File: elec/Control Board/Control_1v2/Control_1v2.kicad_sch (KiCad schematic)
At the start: 166 parts, among them J1 DB9_Female_MountingHoles, J10 Conn_02x12_Odd_Even, J11 Screw_Terminal_01x02, J14 Conn_01x10, J2 Conn_01x08, J25 Screw_Terminal_01x02, J26 Conn_01x10, J27 Conn_02x12_Odd_Even, J28 Screw_Terminal_01x02, J29 Conn_01x10, J3 Conn_01x08, J37 Conn_01x04, J4 Conn_01x08, J5 Conn_01x08, J6 Conn_01x08, J7 Conn_01x10, J8 Conn_02x18_Odd_Even, J9 Conn_01x10, Q601 BSS138

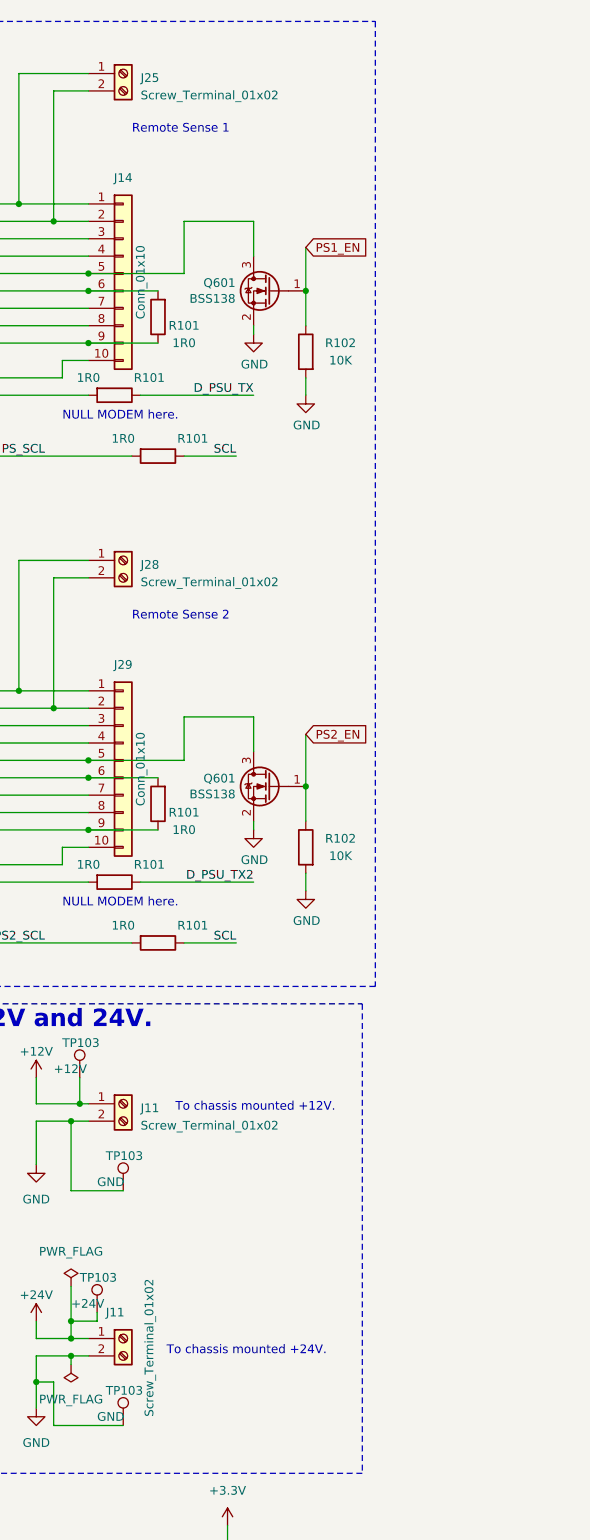
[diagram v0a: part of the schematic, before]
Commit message: Update Control_1v2.kicad_sch for correct JLCPCB part number on JST 2 pin XH Connector. Wire up J30 as connector for OEDCS Fan.
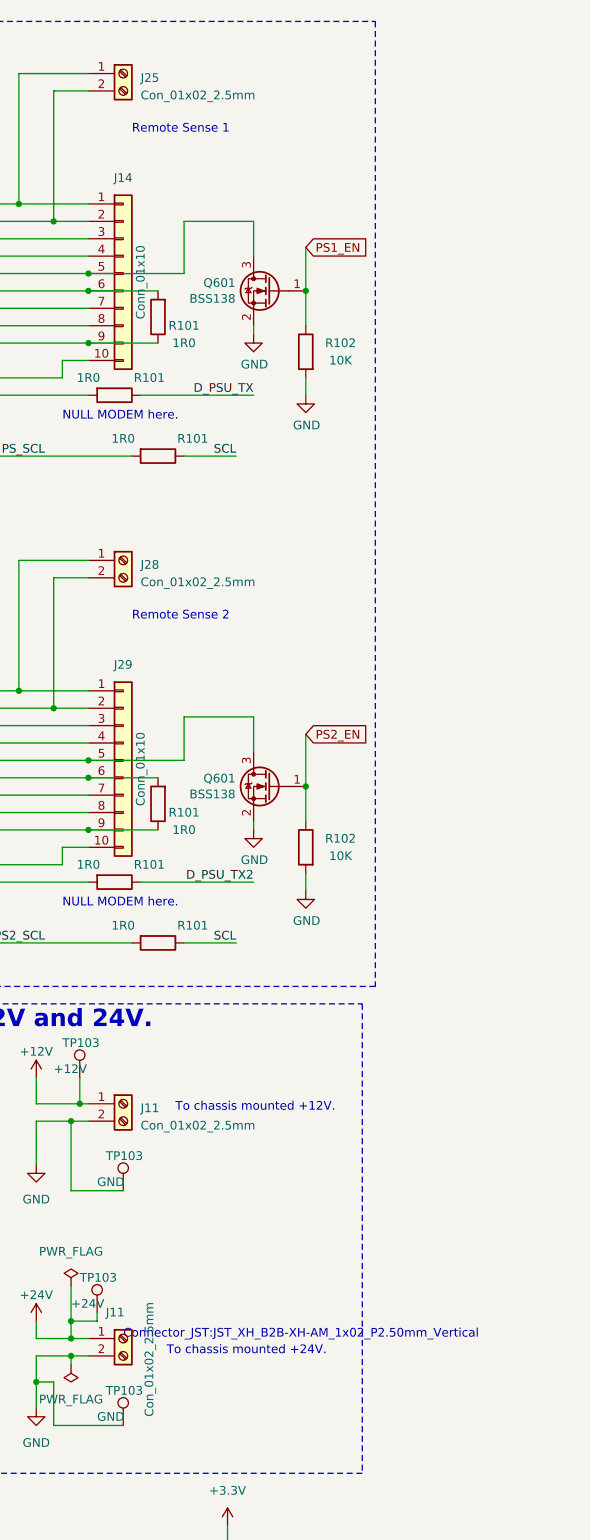
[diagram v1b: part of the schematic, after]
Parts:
- J11, J25, J28: value Screw_Terminal_01x02 -> Con_01x02_2.5mm; footprint TerminalBlock_TE-Connectivity:TerminalBlock_TE_282834-2_1x02_P2.54mm_Horizontal -> Connector_JST:JST_XH_B2B-XH-AM_1x02_P2.50mm_Vertical; Cost 0.1537 -> 0.2156; MPN DB125-2.54-2P-GN-S -> B2B-XH-A-GU; Manufacturer DIBO -> JST
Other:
- note added: "Connector_JST:JST_XH_B2B-XH-AM_1x02_P2.50mm_Vertical"
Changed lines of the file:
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@@
     (effects (font (size 2.54 2.54)) (justify left bottom))
   )
+  (text "Connector_JST:JST_XH_B2B-XH-AM_1x02_P2.50mm_Vertical\n"
+    (at 482.6 206.502 0)
+    (effects (font (size 1.27 1.27)) (justify left bottom))
+  )
   (text "V_ASSY_VERSIONING\nControl 1.2 voltage = 1.055V" (at 124.714 137.414 0)
     (effects (font (size 1.27 1.27)) (justify left bottom))
@@
       (effects (font (size 1.27 1.27)) (justify left))
     )
-    (property "Value" "Screw_Terminal_01x02" (at 486.41 217.805 90)
+    (property "Value" "Con_01x02_2.5mm" (at 486.41 217.805 90)
       (effects (font (size 1.27 1.27)) (justify left))
     )
-    (property "Footprint" "TerminalBlock_TE-Connectivity:TerminalBlock_TE_282834-2_1x02_P2.54mm_Horizontal" (at 482.6 206.375 0)
+    (property "Footprint" "Connector_JST:JST_XH_B2B-XH-AM_1x02_P2.50mm_Vertical" (at 482.6 206.375 0)
       (effects (font (size 1.27 1.27)) hide)
     )
@@
       (effects (font (size 1.27 1.27)) hide)
     )
-    (property "Cost" "0.1537" (at 482.6 206.375 0)
+    (property "Cost" "0.2156" (at 482.6 206.375 0)
       (effects (font (size 1.27 1.27)) hide)
     )
-    (property "Description" "1x2P XH 1 2.5mm 2 Brass Plugin,P=2.5mm Wire To Board / Wire To Wire Connector ROHS" (at 482.6 206.375 0)
+    (property "Description" "1x2P 2P XH Gold 2 -25℃~+85℃ 3A 1 2.5mm Brass Direct Insert Plugin,P=2.5mm Wire To Board Connector ROHS" (at 482.6 206.375 0)
       (effects (font (size 1.27 1.27)) hide)
     )
@@
       (effects (font (size 1.27 1.27)) hide)
     )
-    (property "MPN" "DB125-2.54-2P-GN-S" (at 482.6 206.375 0)
+    (property "MPN" "B2B-XH-A-GU" (at 482.6 206.375 0)
       (effects (font (size 1.27 1.27)) hide)
     )
-    (property "Manufacturer" "DIBO" (at 482.6 206.375 0)
+    (property "Manufacturer" "JST" (at 482.6 206.375 0)
       (effects (font (size 1.27 1.27)) hide)
     )
@@
       (effects (font (size 1.27 1.27)) (justify left))
     )
-    (property "Value" "Screw_Terminal_01x02" (at 485.14 175.26 0)
+    (property "Value" "Con_01x02_2.5mm" (at 485.14 175.26 0)
       (effects (font (size 1.27 1.27)) (justify left))
     )
-    (property "Footprint" "TerminalBlock_TE-Connectivity:TerminalBlock_TE_282834-2_1x02_P2.54mm_Horizontal" (at 482.6 172.085 0)
+    (property "Footprint" "Connector_JST:JST_XH_B2B-XH-AM_1x02_P2.50mm_Vertical" (at 482.6 172.085 0)
       (effects (font (size 1.27 1.27)) hide)
     )
@@
       (effects (font (size 1.27 1.27)) hide)
     )
-    (property "Cost" "0.1537" (at 482.6 172.085 0)
+    (property "Cost" "0.2156" (at 482.6 172.085 0)
       (effects (font (size 1.27 1.27)) hide)
     )
-    (property "Description" "1x2P XH 1 2.5mm 2 Brass Plugin,P=2.5mm Wire To Board / Wire To Wire Connector ROHS" (at 482.6 172.085 0)
+    (property "Description" "1x2P 2P XH Gold 2 -25℃~+85℃ 3A 1 2.5mm Brass Direct Insert Plugin,P=2.5mm Wire To Board Connector ROHS" (at 482.6 172.085 0)
       (effects (font (size 1.27 1.27)) hide)
     )
@@
       (effects (font (size 1.27 1.27)) hide)
     )
-    (property "MPN" "DB125-2.54-2P-GN-S" (at 482.6 172.085 0)
+    (property "MPN" "B2B-XH-A-GU" (at 482.6 172.085 0)
       (effects (font (size 1.27 1.27)) hide)
     )
-    (property "Manufacturer" "DIBO" (at 482.6 172.085 0)
+    (property "Manufacturer" "JST" (at 482.6 172.085 0)
       (effects (font (size 1.27 1.27)) hide)
     )
@@
       (effects (font (size 1.27 1.27)) (justify left))
     )
-    (property "Value" "Screw_Terminal_01x02" (at 485.14 24.765 0)
+    (property "Value" "Con_01x02_2.5mm" (at 485.14 24.765 0)
       (effects (font (size 1.27 1.27)) (justify left))
     )
-    (property "Footprint" "TerminalBlock_TE-Connectivity:TerminalBlock_TE_282834-2_1x02_P2.54mm_Horizontal" (at 482.6 21.59 0)
+    (property "Footprint" "Connector_JST:JST_XH_B2B-XH-AM_1x02_P2.50mm_Vertical" (at 482.6 21.59 0)
       (effects (font (size 1.27 1.27)) hide)
     )
@@
       (effects (font (size 1.27 1.27)) hide)
     )
-    (property "Cost" "0.1537" (at 482.6 21.59 0)
+    (property "Cost" "0.2156" (at 482.6 21.59 0)
       (effects (font (size 1.27 1.27)) hide)
     )
-    (property "Description" "1x2P XH 1 2.5mm 2 Brass Plugin,P=2.5mm Wire To Board / Wire To Wire Connector ROHS" (at 482.6 21.59 0)
+    (property "Description" "1x2P 2P XH Gold 2 -25℃~+85℃ 3A 1 2.5mm Brass Direct Insert Plugin,P=2.5mm Wire To Board Connector ROHS" (at 482.6 21.59 0)
       (effects (font (size 1.27 1.27)) hide)
     )
@@
       (effects (font (size 1.27 1.27)) hide)
     )
-    (property "MPN" "DB125-2.54-2P-GN-S" (at 482.6 21.59 0)
+    (property "MPN" "B2B-XH-A-GU" (at 482.6 21.59 0)
       (effects (font (size 1.27 1.27)) hide)
     )
-    (property "Manufacturer" "DIBO" (at 482.6 21.59 0)
+    (property "Manufacturer" "JST" (at 482.6 21.59 0)
       (effects (font (size 1.27 1.27)) hide)
     )
@@
       (effects (font (size 1.27 1.27)) (justify left))
     )
-    (property "Value" "Screw_Terminal_01x02" (at 485.14 95.885 0)
+    (property "Value" "Con_01x02_2.5mm" (at 485.14 95.885 0)
       (effects (font (size 1.27 1.27)) (justify left))
     )
-    (property "Footprint" "TerminalBlock_TE-Connectivity:TerminalBlock_TE_282834-2_1x02_P2.54mm_Horizontal" (at 482.6 92.71 0)
+    (property "Footprint" "Connector_JST:JST_XH_B2B-XH-AM_1x02_P2.50mm_Vertical" (at 482.6 92.71 0)
       (effects (font (size 1.27 1.27)) hide)
     )
@@
       (effects (font (size 1.27 1.27)) hide)
     )
-    (property "Cost" "0.1537" (at 482.6 92.71 0)
+    (property "Cost" "0.2156" (at 482.6 92.71 0)
       (effects (font (size 1.27 1.27)) hide)
     )
-    (property "Description" "1x2P XH 1 2.5mm 2 Brass Plugin,P=2.5mm Wire To Board / Wire To Wire Connector ROHS" (at 482.6 92.71 0)
+    (property "Description" "1x2P 2P XH Gold 2 -25℃~+85℃ 3A 1 2.5mm Brass Direct Insert Plugin,P=2.5mm Wire To Board Connector ROHS" (at 482.6 92.71 0)
       (effects (font (size 1.27 1.27)) hide)
     )
@@
       (effects (font (size 1.27 1.27)) hide)
     )
-    (property "MPN" "DB125-2.54-2P-GN-S" (at 482.6 92.71 0)
+    (property "MPN" "B2B-XH-A-GU" (at 482.6 92.71 0)
       (effects (font (size 1.27 1.27)) hide)
     )
-    (property "Manufacturer" "DIBO" (at 482.6 92.71 0)
+    (property "Manufacturer" "JST" (at 482.6 92.71 0)
       (effects (font (size 1.27 1.27)) hide)
     )

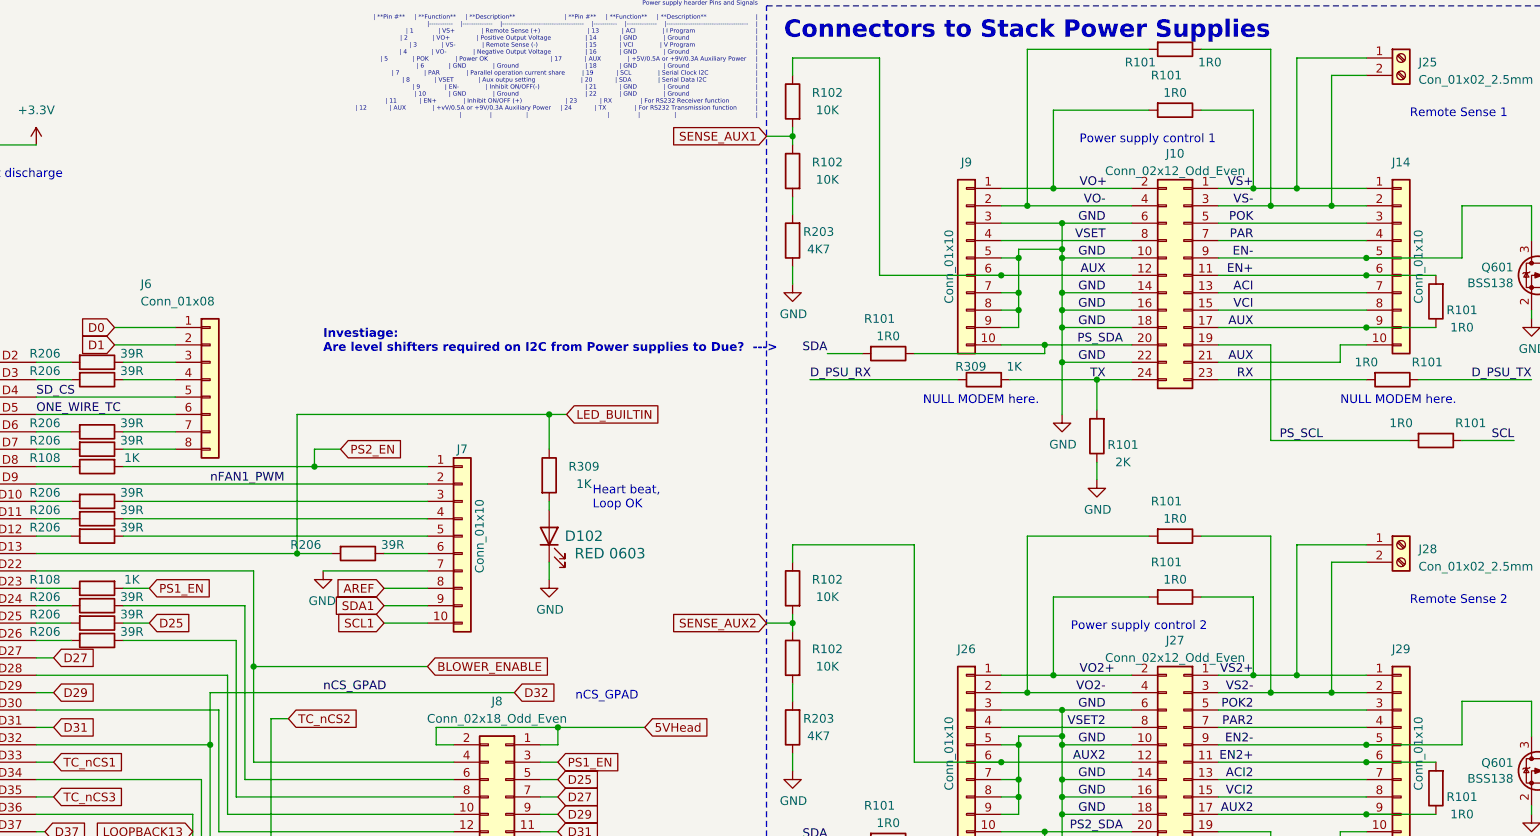
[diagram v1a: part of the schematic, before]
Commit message: Update Control_1v2.kicad_sch for Power OK from power supply into Due for possible interupt service of power supply NOT OK.
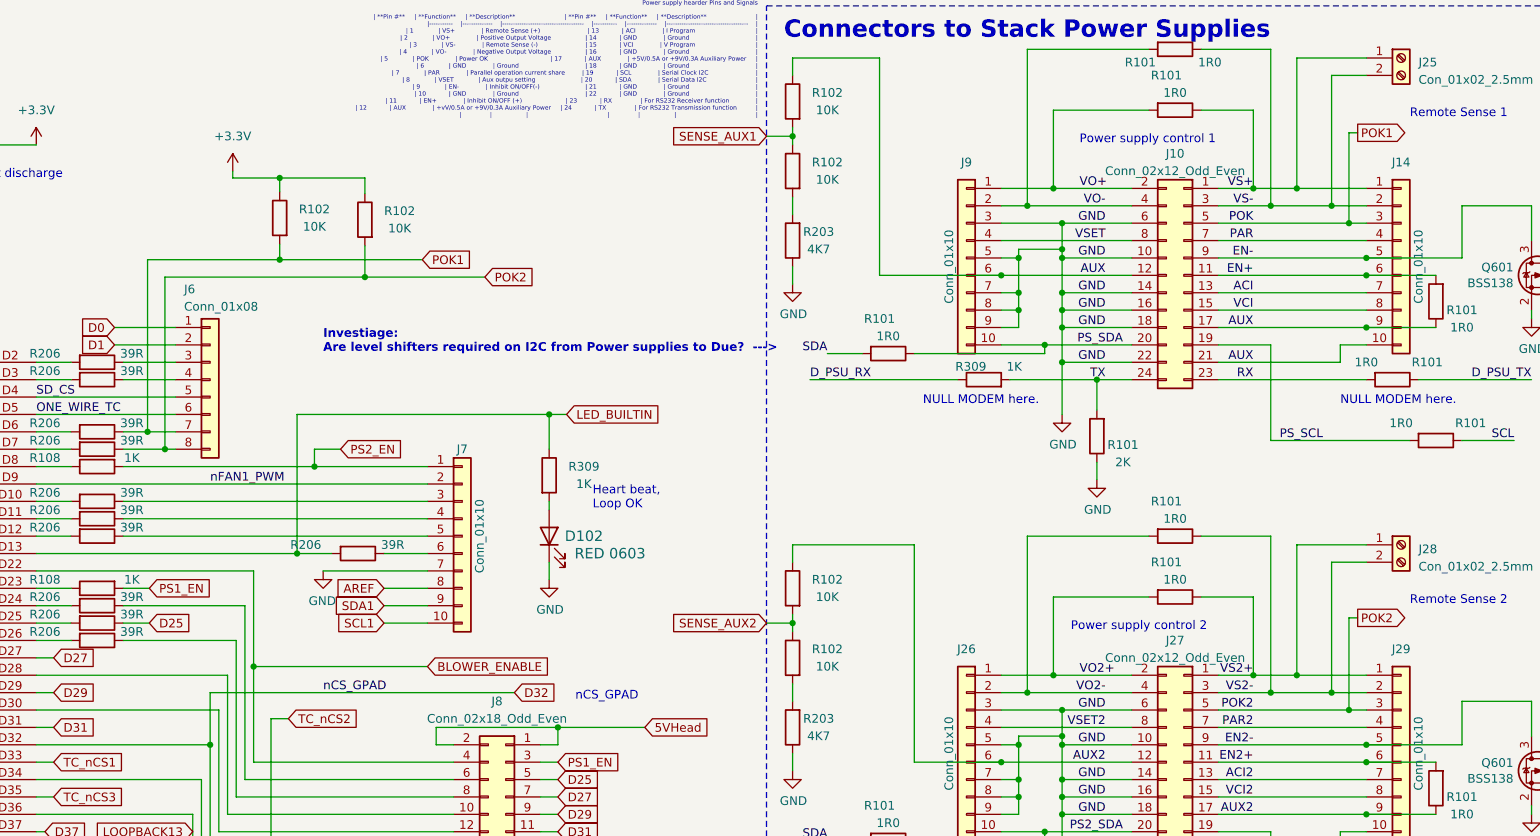
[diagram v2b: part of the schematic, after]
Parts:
- added R102 (x2): 10K, Resistor_SMD:R_0603_1608Metric_Pad0.98x0.95mm_HandSolder, symbol Device:R
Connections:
- net POK is gone; now on net POK1: J10.5 (Pin_5), J14.3 (Pin_3)
- net +3.3V: now also R102.1, R102.1
- net POK2: now also J6.8 (Pin_8), R206.1, R102.2
- net POK1: now reaches J6.7 (Pin_7), R206.1
- net POK1: now also R102.2

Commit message: Clearing more ERC schematic errors. Off grid. Remove some redundant Net names.
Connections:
- net D49 renamed SHUTDOWN
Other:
- sheet Display Interface ports: added +12V_RELAY, +5V_RELAY; removed none
- note added: "LOOPBACK25"
- moved on the sheet: J11, J37, R101, R102, R203, TP103

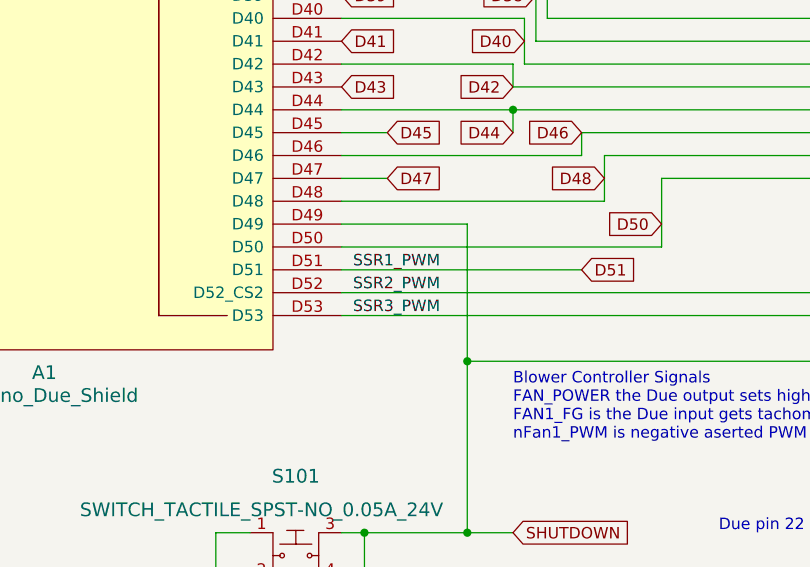
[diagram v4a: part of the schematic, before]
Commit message: Clearing more ERC schematic errors. Only errors related to libraries and ground symbol modified remain.
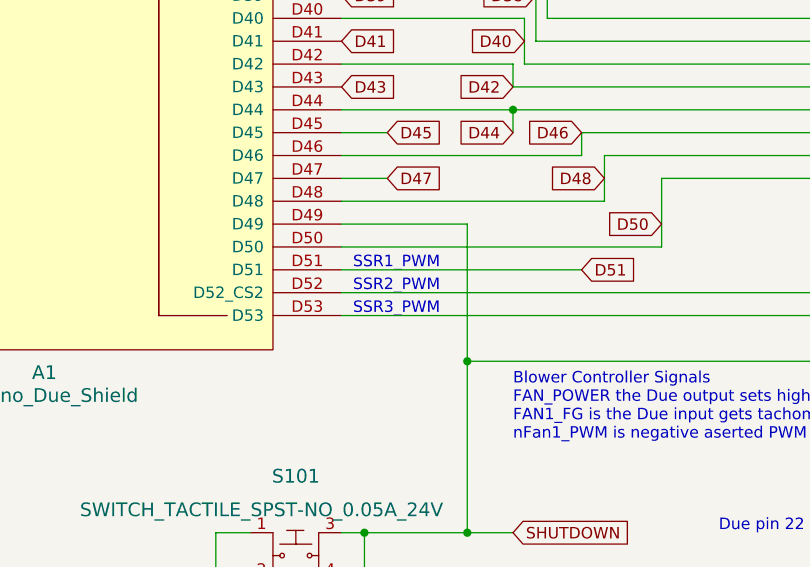
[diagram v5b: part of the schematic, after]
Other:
- note added: "SSR1_PWM"
- note added: "SSR2_PWM"
- note added: "SSR3_PWM"
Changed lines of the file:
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@@
+    (effects (font (size 1.27 1.27)) (justify left bottom))
+  )
+  (text "SSR2_PWM" (at 284.48 172.72 0)
     (effects (font (size 1.27 1.27)) (justify left bottom))
   )
@@
   )
   (text "To chassis mounted +12V." (at 490.22 173.355 0)
+    (effects (font (size 1.27 1.27)) (justify left bottom))
+  )
+  (text "SSR3_PWM" (at 284.48 175.26 0)
     (effects (font (size 1.27 1.27)) (justify left bottom))
   )
@@
     (effects (font (size 1.27 1.27)) (justify left bottom))
   )
+  (text "SSR1_PWM" (at 284.48 170.18 0)
+    (effects (font (size 1.27 1.27)) (justify left bottom))
+  )
   (text "V_ASSY_VERSIONING\nControl 1.2 voltage = 1.055V" (at 124.714 137.414 0)
     (effects (font (size 1.27 1.27)) (justify left bottom))
@@
     (effects (font (size 1.27 1.27)) (justify right bottom))
   )
-  (label "SSR1_PWM" (at 284.48 170.18 0) (fields_autoplaced)
-    (effects (font (size 1.27 1.27)) (justify left bottom))
-  )
   (label "D_PSU_RX2" (at 396.24 139.7 0) (fields_autoplaced)
     (effects (font (size 1.27 1.27)) (justify left bottom))
@@
     (effects (font (size 1.27 1.27)) (justify right bottom))
   )
-  (label "SSR2_PWM" (at 284.48 172.72 0) (fields_autoplaced)
-    (effects (font (size 1.27 1.27)) (justify left bottom))
-  )
   (label "SDA" (at 398.78 64.77 180) (fields_autoplaced)
     (effects (font (size 1.27 1.27)) (justify right bottom))
@@
     (effects (font (size 1.27 1.27)) (justify right bottom))
   )
-  (label "SSR3_PWM" (at 284.48 175.26 0) (fields_autoplaced)
-    (effects (font (size 1.27 1.27)) (justify left bottom))
-  )
   (label "PS2_SDA" (at 441.96 134.62 180) (fields_autoplaced)

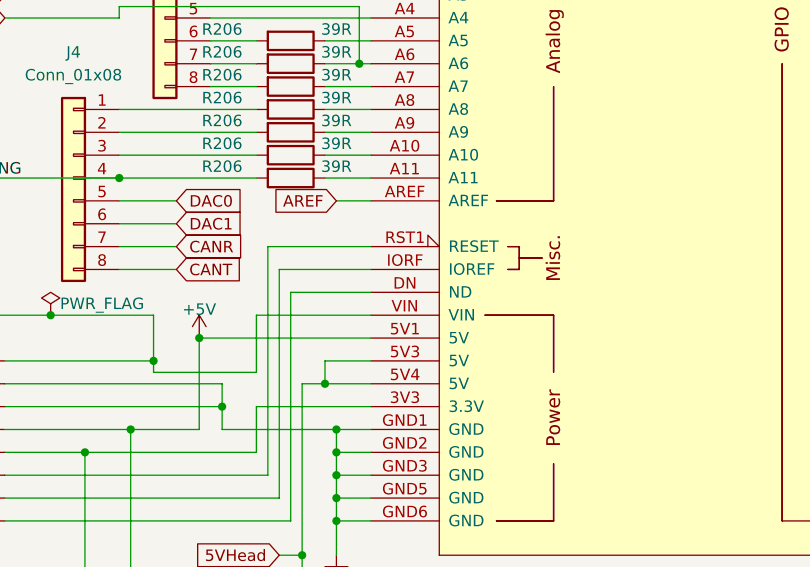
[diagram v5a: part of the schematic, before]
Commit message: PCB V1.2. Routing with out errors.
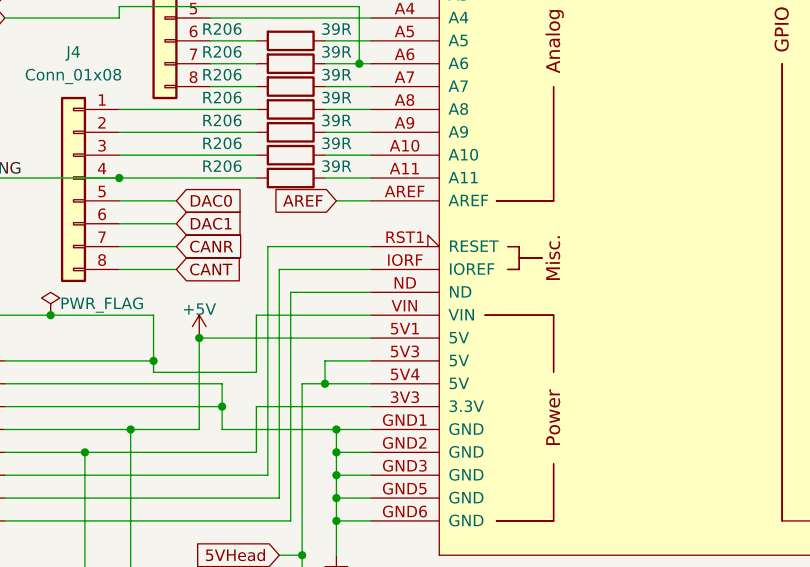
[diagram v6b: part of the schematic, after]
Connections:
- net at J3.8 (Pin_8): now also A1.ND; no longer A1.DN (ND)
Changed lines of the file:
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@@
     (pin "DAC0")
     (pin "DAC1")
-    (pin "DN")
+    (pin "ND")
     (pin "GND1")
     (pin "GND2")
